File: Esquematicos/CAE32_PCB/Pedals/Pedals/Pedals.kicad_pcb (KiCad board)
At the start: 4 copper layers, 45 x 55 mm, 34 parts, among them U1 STM32G070RBT6, U2 LDL1117, U3 HX711, U4 STM32F072RBTx, U5 ADC128S102

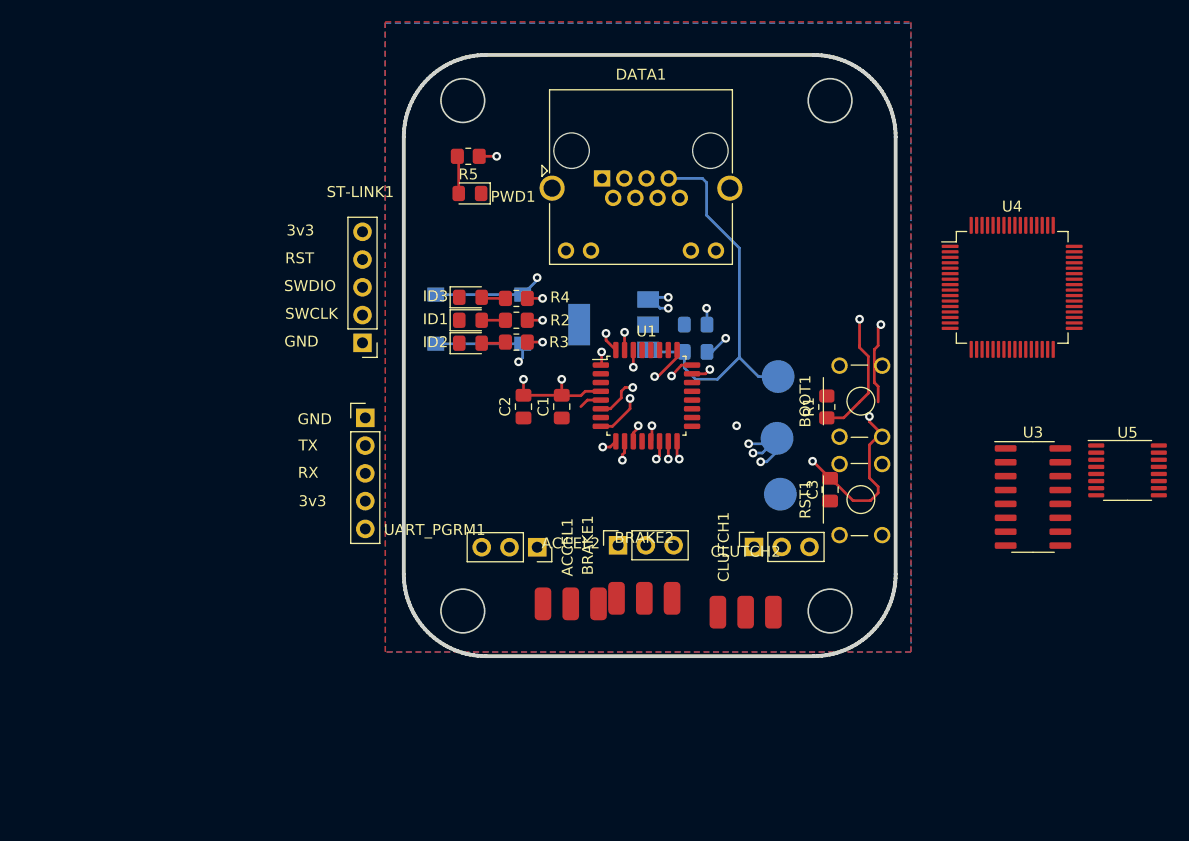
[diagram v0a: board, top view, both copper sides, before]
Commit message: chore: se corrigen valores de referencias de componentes, creación de nuevas hojas de diagramas, mejor distribución de componentes
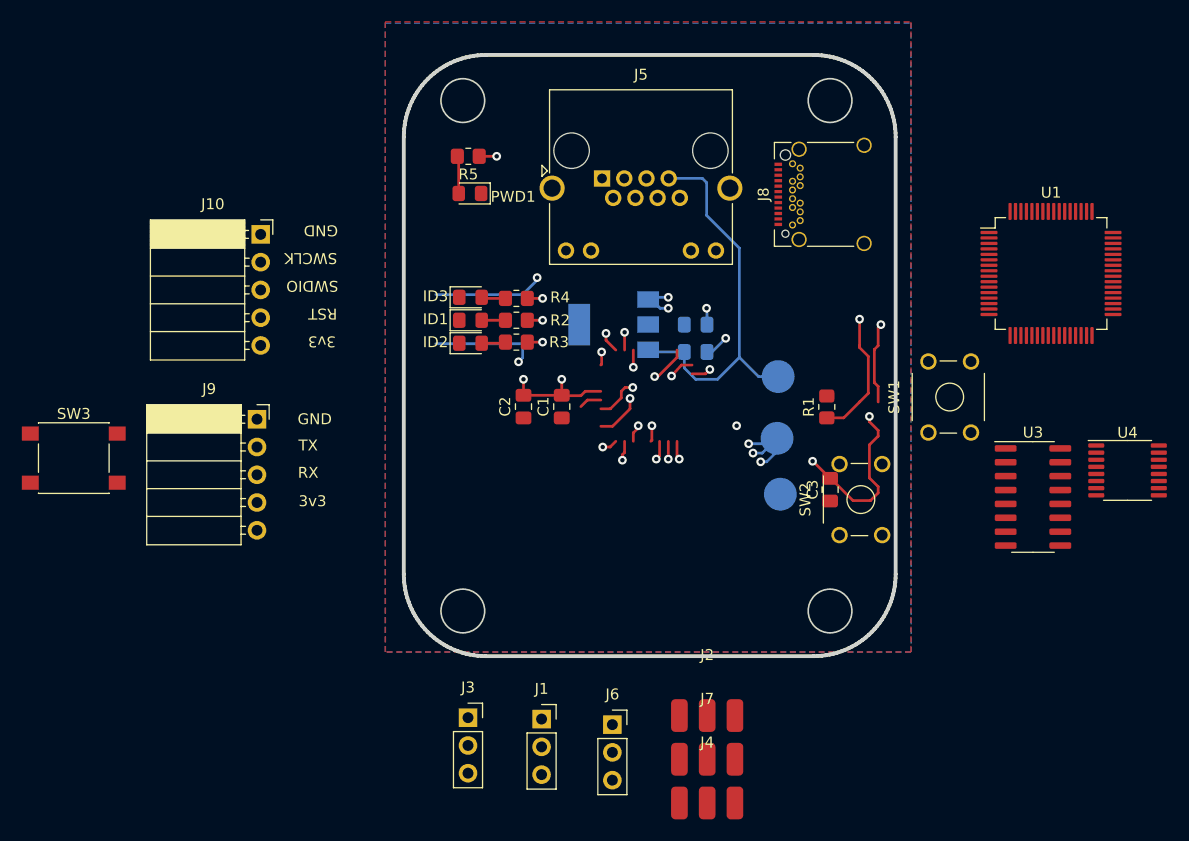
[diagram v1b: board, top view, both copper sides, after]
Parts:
- removed ACCEL1, BRAKE1, CLUTCH1: Conn_01x03_Female, Connector_PinSocket_2.54mm:PinSocket_1x03_P2.54mm_Vertical
- removed ACCEL2, BRAKE2, CLUTCH2: Conn_01x03_Female, Extra_components:1x3_pin
- removed MODE1: SW_Push, Button_Switch_SMD:SW_Push_1P1T_NO_6x6mm_H9.5mm
- removed ST-LINK1, UART_PGRM1: Conn_01x05_Female, Connector_PinHeader_2.54mm:PinHeader_1x05_P2.54mm_Vertical
- removed the U1 at (146.5, 103.0)
- added J1: Conn_01x03_Female, Connector_PinSocket_2.54mm:PinSocket_1x03_P2.54mm_Vertical, F.Cu at (136.9, 132.6)
- added J10: ST-Link, Connector_PinSocket_2.54mm:PinSocket_1x05_P2.54mm_Horizontal, F.Cu at (111.2, 88.2)
- added J2: Conn_01x03_Female, Extra_components:1x3_pin, F.Cu at (152.1, 132.3)
- added J3: Conn_01x03_Female, Connector_PinSocket_2.54mm:PinSocket_1x03_P2.54mm_Vertical, F.Cu at (130.2, 132.5)
- added J4: Conn_01x03_Female, Extra_components:1x3_pin, F.Cu at (152.1, 140.3)
- added J6: Conn_01x03_Female, Connector_PinSocket_2.54mm:PinSocket_1x03_P2.54mm_Vertical, F.Cu at (143.4, 133.1)
- added J7: Conn_01x03_Female, Extra_components:1x3_pin, F.Cu at (152.1, 136.3)
- added J8: USB_C_Receptacle, Connector_USB:USB_C_Receptacle_Amphenol_12401548E4-2A_CircularHoles, F.Cu at (163.6, 84.6)
- added J9: UART_PGR, Connector_PinSocket_2.54mm:PinSocket_1x05_P2.54mm_Horizontal, F.Cu at (110.9, 105.2)
- added SW3: MODE, Button_Switch_SMD:SW_Push_1P1T_NO_6x6mm_H9.5mm, F.Cu at (94.1, 108.7)
- J5: renamed from DATA1; value 8P8C_LED_Shielded -> PGRM and SPI
- SW1: renamed from BOOT1; value SW_Push -> BOOT
- SW2: renamed from RST1; value SW_Push -> RST
- moved SW1 8.14 mm to (174.2, 103.1)
- moved U1 3.78 mm to (183.5, 91.8)
- renumbered GND1 to TP1, 5V1 to TP2, 3v3 to TP3, U4 to U1, U5 to U4
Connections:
- U1 pad 50: /PSK -> unconnected-(U1-Pad50)
- U1 pad 57: /sd -> unconnected-(U1-Pad57)
- U3 pad 11: /sd -> unconnected-(U3-Pad11)
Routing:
- net (no net): track 0.00 -> 61.3 mm, vias 0 -> 3
- net /SWDIO: track 24.0 -> 0.00 mm, vias 1 -> 0
- net /USART_RX: track 19.5 -> 0.00 mm, vias 1 -> 0
- net GNDREF: track 28.9 -> 48.0 mm, vias 8 -> 9
- net /ACCEL: track 19.1 -> 0.00 mm, vias 1 -> 0
- net /USART_TX: track 17.8 -> 0.00 mm, vias 1 -> 0
- net Net-(J8-PadA1): track 0.00 -> 10.6 mm, vias 0 -> 1
- net /BRAKE: track 10.6 -> 0.00 mm, vias 1 -> 0

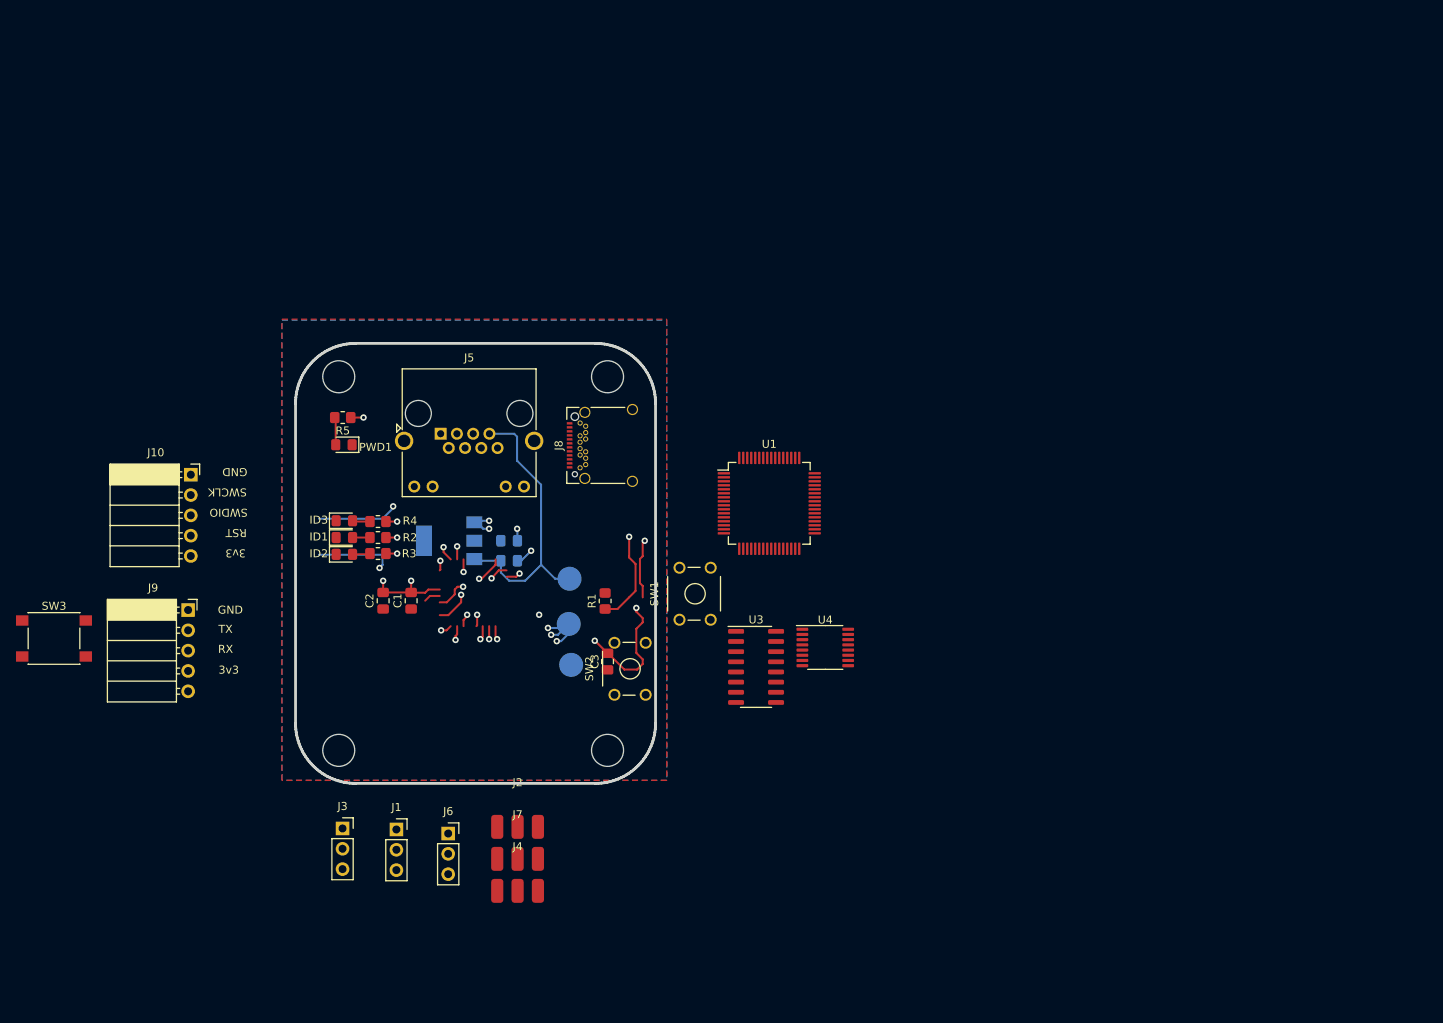
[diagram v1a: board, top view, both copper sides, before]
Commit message: update: Primera revision de etapa ADC lista, ademas de una mejor distrubucion de componentes
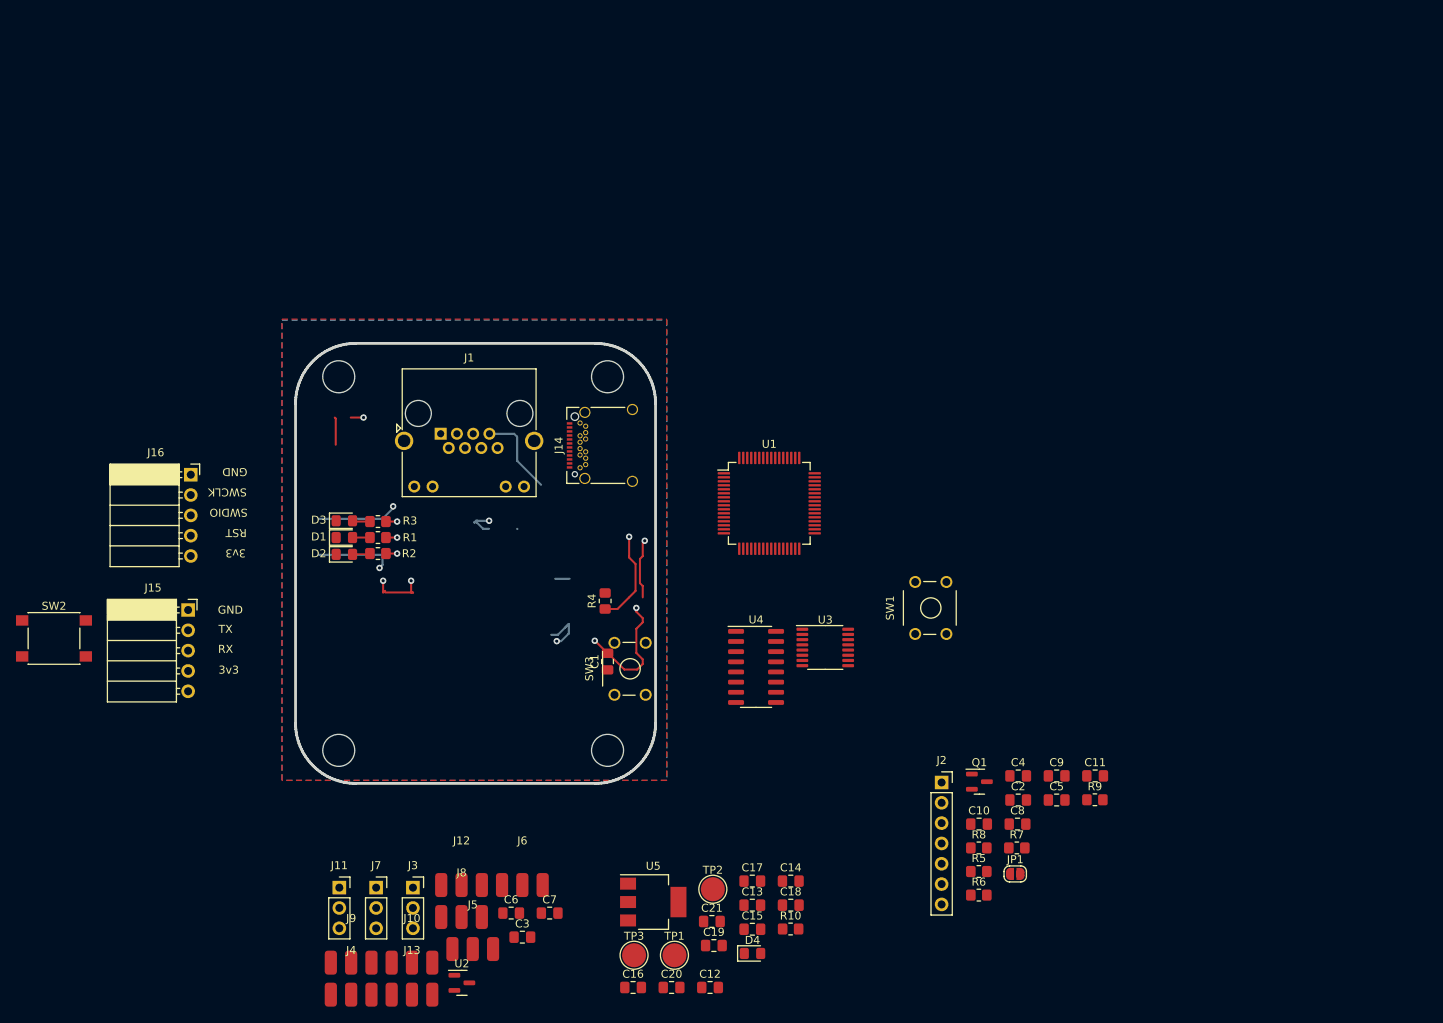
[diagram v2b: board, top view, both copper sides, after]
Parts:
- removed the C1 at (138.8, 104.0)
- removed the J1 at (136.9, 132.6)
- removed PWD1: LED, LED_SMD:LED_0805_2012Metric_Pad1.15x1.40mm_HandSolder
- added C10: 0u1, Capacitor_SMD:C_0805_2012Metric_Pad1.18x1.45mm_HandSolder, F.Cu at (209.7, 131.9)
- added C11: 10u, Capacitor_SMD:C_0805_2012Metric_Pad1.18x1.45mm_HandSolder, F.Cu at (224.2, 125.9)
- added C12: 1uf, Capacitor_SMD:C_0805_2012Metric_Pad1.18x1.45mm_HandSolder, F.Cu at (176.1, 152.3)
- added C13: 4.7uf, Capacitor_SMD:C_0805_2012Metric_Pad1.18x1.45mm_HandSolder, F.Cu at (181.4, 142.1)
- added C14: 100n, Capacitor_SMD:C_0805_2012Metric_Pad1.18x1.45mm_HandSolder, F.Cu at (186.2, 139.0)
- added C15: 100n, Capacitor_SMD:C_0805_2012Metric_Pad1.18x1.45mm_HandSolder, F.Cu at (181.4, 145.1)
- added C16: 100n, Capacitor_SMD:C_0805_2012Metric_Pad1.18x1.45mm_HandSolder, F.Cu at (166.5, 152.3)
- added C17: 100n, Capacitor_SMD:C_0805_2012Metric_Pad1.18x1.45mm_HandSolder, F.Cu at (181.4, 139.0)
- added C18: 10n, Capacitor_SMD:C_0805_2012Metric_Pad1.18x1.45mm_HandSolder, F.Cu at (186.2, 142.1)
- added C19: 1u, Capacitor_SMD:C_0805_2012Metric_Pad1.18x1.45mm_HandSolder, F.Cu at (176.6, 147.1)
- added C20: 4u7, Capacitor_SMD:C_0805_2012Metric_Pad1.18x1.45mm_HandSolder, F.Cu at (171.3, 152.3)
- added C21: 4u7, Capacitor_SMD:C_0805_2012Metric_Pad1.18x1.45mm_HandSolder, F.Cu at (176.3, 144.1)
- added C3: 47u, Capacitor_SMD:C_0805_2012Metric_Pad1.18x1.45mm_HandSolder, F.Cu at (152.7, 146.1)
- added C6: 0u1, Capacitor_SMD:C_0805_2012Metric_Pad1.18x1.45mm_HandSolder, F.Cu at (151.3, 143.0)
- added C7: 0u1, Capacitor_SMD:C_0805_2012Metric_Pad1.18x1.45mm_HandSolder, F.Cu at (156.1, 143.0)
- added C8: 0u1, Capacitor_SMD:C_0805_2012Metric_Pad1.18x1.45mm_HandSolder, F.Cu at (214.6, 131.9)
- added C9: 0u1, Capacitor_SMD:C_0805_2012Metric_Pad1.18x1.45mm_HandSolder, F.Cu at (219.4, 125.9)
- added D4: PWR, LED_SMD:LED_0805_2012Metric_Pad1.15x1.40mm_HandSolder, F.Cu at (181.4, 148.1)
- added J10: Conn_01x03_Female, Extra_components:1x3_pin, F.Cu at (138.9, 149.2)
- added J11: Conn_01x03_Female, Connector_PinSocket_2.54mm:PinSocket_1x03_P2.54mm_Vertical, F.Cu at (129.8, 139.9)
- added J12: Conn_01x03_Female, Extra_components:1x3_pin, F.Cu at (145.1, 139.5)
- added J13: Conn_01x03_Female, Extra_components:1x3_pin, F.Cu at (138.9, 153.2)
- added J5: Conn_01x03_Female, Extra_components:1x3_pin, F.Cu at (146.5, 147.5)
- added J8: Conn_01x03_Female, Extra_components:1x3_pin, F.Cu at (145.1, 143.5)
- added J9: Conn_01x03_Female, Extra_components:1x3_pin, F.Cu at (131.3, 149.2)
- added JP1: SolderJumper_2_Open, Jumper:SolderJumper-2_P1.3mm_Open_RoundedPad1.0x1.5mm, F.Cu at (214.3, 138.1)
- added Q1: MMBT3906, Package_TO_SOT_SMD:SOT-23, F.Cu at (209.8, 126.6)
- added R10: 43, Resistor_SMD:R_0805_2012Metric_Pad1.20x1.40mm_HandSolder, F.Cu at (186.2, 145.0)
- added R6: 100, Resistor_SMD:R_0805_2012Metric_Pad1.20x1.40mm_HandSolder, F.Cu at (209.7, 140.8)
- added R7: 20k, Resistor_SMD:R_0805_2012Metric_Pad1.20x1.40mm_HandSolder, F.Cu at (214.5, 134.9)
- added R8: 8.2k, Resistor_SMD:R_0805_2012Metric_Pad1.20x1.40mm_HandSolder, F.Cu at (209.7, 134.9)
- added R9: 10k, Resistor_SMD:R_0805_2012Metric_Pad1.20x1.40mm_HandSolder, F.Cu at (224.2, 128.9)
- added U5: LDL1117, Package_TO_SOT_SMD:SOT-223-3_TabPin2, F.Cu at (169.0, 141.7)
- C2: value 4.7uf -> 0u1
- C4: value 1uf -> 0u1; moved to F.Cu
- C5: value 4.7uf -> 10u; moved to F.Cu
- D1: renamed from ID1; value LED -> LED_1
- D2: renamed from ID2; value LED -> LED_2
- D3: renamed from ID3; value LED -> LED_3
- J2: value Conn_01x03_Female -> Conn_01x07_Female; footprint Extra_components:1x3_pin -> Connector_PinSocket_2.54mm:PinSocket_1x07_P2.54mm_Vertical
- J6: footprint Connector_PinSocket_2.54mm:PinSocket_1x03_P2.54mm_Vertical -> Extra_components:1x3_pin
- J7: footprint Extra_components:1x3_pin -> Connector_PinSocket_2.54mm:PinSocket_1x03_P2.54mm_Vertical
- R5: value 43 -> 100
- TP1, TP2, TP3: moved to F.Cu
- U2: value LDL1117 -> REF3033; footprint Package_TO_SOT_SMD:SOT-223-3_TabPin2 -> Package_TO_SOT_SMD:SOT-23; moved to F.Cu
- moved R5 97.7 mm to (209.7, 137.8), turned to 0 degrees
- moved C2 83.2 mm to (214.6, 128.9), turned to 0 degrees
- moved C5 75.7 mm to (219.4, 128.9)
- moved C4 69.1 mm to (214.6, 125.9)
- moved U2 55.3 mm to (145.1, 151.8), turned to 0 degrees
- moved J2 53.3 mm to (205.1, 126.7)
- moved TP1 43.5 mm to (171.7, 148.3), turned to 0 degrees
- moved TP2 42.7 mm to (176.5, 140.1), turned to 0 degrees
- moved TP3 37.1 mm to (166.6, 148.3), turned to 0 degrees
- moved SW1 29.5 mm to (203.7, 104.9)
- moved J4 24.5 mm to (131.3, 153.2)
- moved J7 18.0 mm to (134.4, 139.9)
- moved J3 11.5 mm to (139.0, 139.9)
- moved J6 11.3 mm to (152.7, 139.5)
- renumbered C3 to C1, J5 to J1, J8 to J14, J9 to J15, J10 to J16, R2 to R1, R3 to R2, R4 to R3, R1 to R4, SW3 to SW2, SW2 to SW3, U4 to U3, U3 to U4
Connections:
- C2 pad 1: GNDREF -> Net-(C2-Pad1)
- C2 pad 2: +3.3V -> unconnected-(C2-Pad2)
- C4 pad 1: +5V -> Net-(U4-Pad8)
- C4 pad 2: GNDREF -> Net-(U4-Pad7)
- C5 pad 1: +3.3V -> Net-(C2-Pad1)
- C5 pad 2: GNDREF -> unconnected-(C5-Pad2)
- J14 pad A1: Net-(J8-PadA1) -> GNDREF
- J14 pad A12: Net-(J8-PadA1) -> GNDREF
- J14 pad A6: unconnected-(J8-PadA6) -> /Connectors(USB,Programming and debugging)/D+
- J14 pad A7: unconnected-(J8-PadA7) -> /Connectors(USB,Programming and debugging)/D-
- J14 pad B1: Net-(J8-PadA1) -> GNDREF
- J14 pad B12: Net-(J8-PadA1) -> GNDREF
- J14 pad B6: unconnected-(J8-PadB6) -> /Connectors(USB,Programming and debugging)/D+
- J14 pad B7: unconnected-(J8-PadB7) -> /Connectors(USB,Programming and debugging)/D-
- J14 pad S1: unconnected-(J8-PadS1) -> GNDREF
- J2 pad 1: +3.3V -> GNDREF
- J2 pad 2: /BRAKE -> /ADCs components/B+
- J2 pad 3: GNDREF -> /ADCs components/B-
- J3 pad 2: /ACCEL -> /ADCs components/BRAKE
- J4 pad 2: /ACCEL -> /ADCs components/BRAKE
- J6 pad 2: /CLUTCH -> /ADCs components/Custom_4
- J7 pad 2: /CLUTCH -> /ADCs components/ACCEL
- R4 pad 1: /SWCLK -> /BOOT
- R5 pad 1: +3.3V -> /ADCs components/A+
- R5 pad 2: Net-(PWD1-Pad2) -> Net-(U4-Pad8)
- SW1 pad 1: +3.3V -> /BOOT
- SW1 pad 2: /SWCLK -> +3.3V
- U1 pad 60: unconnected-(U1-Pad60) -> /BOOT
- U1 pad 7: unconnected-(U1-Pad7) -> /NRST
- U2 pad 1: GNDREF -> +5V
- U2 pad 2: +3.3V -> Net-(U3-Pad2)
- U2 pad 3: +5V -> GNDREF
- U3 pad 1: unconnected-(U4-Pad1) -> /ADCs components/CS
- U3 pad 10: unconnected-(U4-Pad10) -> /ADCs components/Custom_2
- U3 pad 11: unconnected-(U4-Pad11) -> /ADCs components/Custom_1
- U3 pad 12: unconnected-(U4-Pad12) -> GNDREF
- U3 pad 13: unconnected-(U4-Pad13) (its old number) -> +3.3V
- U3 pad 14: unconnected-(U4-Pad14) -> /ADCs components/DIN
- U3 pad 15: unconnected-(U4-Pad15) -> /ADCs components/DOUT
- U3 pad 16: unconnected-(U4-Pad16) -> /ADCs components/SCLK
- U3 pad 2: unconnected-(U4-Pad2) -> Net-(U3-Pad2)
- U3 pad 3: unconnected-(U4-Pad3) -> GNDREF
- U3 pad 4: unconnected-(U4-Pad4) -> /ADCs components/BRAKE
- U3 pad 5: unconnected-(U4-Pad5) -> /ADCs components/ACCEL
- U3 pad 6: unconnected-(U4-Pad6) -> /ADCs components/CLUTCH
- U3 pad 7: unconnected-(U4-Pad7) -> /ADCs components/Custom_5
- U3 pad 8: unconnected-(U4-Pad8) -> /ADCs components/Custom_4
- U3 pad 9: unconnected-(U4-Pad9) -> /ADCs components/Custom_3
- U4 pad 1: unconnected-(U3-Pad1) -> +3.3V
- U4 pad 10: unconnected-(U3-Pad10) -> /ADCs components/B+
- U4 pad 11: unconnected-(U3-Pad11) -> /ADCs components/PD_SCK
- U4 pad 12: unconnected-(U3-Pad12) -> /ADCs components/DOUT
- U4 pad 14: unconnected-(U3-Pad14) -> GNDREF
- U4 pad 15: unconnected-(U3-Pad15) -> Net-(U4-Pad15)
- U4 pad 16: unconnected-(U3-Pad16) -> +3.3V
- U4 pad 2: unconnected-(U3-Pad2) -> Net-(U4-Pad2)
- U4 pad 3: unconnected-(U3-Pad3) -> Net-(U4-Pad3)
- U4 pad 4: unconnected-(U3-Pad4) -> Net-(U4-Pad4)
- U4 pad 5: unconnected-(U3-Pad5) -> GNDREF
- U4 pad 6: unconnected-(U3-Pad6) -> Net-(U4-Pad6)
- U4 pad 7: unconnected-(U3-Pad7) -> Net-(U4-Pad7)
- U4 pad 8: unconnected-(U3-Pad8) -> Net-(U4-Pad8)
- U4 pad 9: unconnected-(U3-Pad9) -> /ADCs components/B-
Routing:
- net /SWCLK: track 42.2 -> 0.00 mm, vias 2 -> 0
- net (no net): track 61.3 -> 19.2 mm, vias 3 -> 0
- net /BOOT: track 0.00 -> 27.4 mm, vias 0 -> 1
- net +5V: track 35.8 -> 12.7 mm
- net /NRST: track 58.3 -> 36.9 mm, vias 3 -> 2
- net /SCKL: track 42.5 -> 23.4 mm, vias 2 -> 0
- net GNDREF: track 48.0 -> 30.4 mm, vias 9 -> 3
- net /IND1: track 18.8 -> 1.40 mm, vias 2 -> 1
- net /CS_PDL: track 24.9 -> 8.18 mm, vias 1 -> 0
- net /MOSI: track 30.5 -> 14.9 mm, vias 1 -> 0
- net /CLUTCH: track 15.0 -> 0.00 mm, vias 1 -> 0
- net /MISO: track 40.5 -> 26.8 mm, vias 1 -> 0
- net /IND0: track 13.1 -> 1.40 mm, vias 2 -> 1
- net Net-(J8-PadA1): track 10.6 -> 0.00 mm, vias 1 -> 0
- net /MODE: track 20.6 -> 13.3 mm, vias 2 -> 1
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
